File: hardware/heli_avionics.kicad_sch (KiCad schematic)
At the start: 13 parts, among them J1 UPDI, SW1 Reset, U1 ATmega4808-A, U5 BMP390L

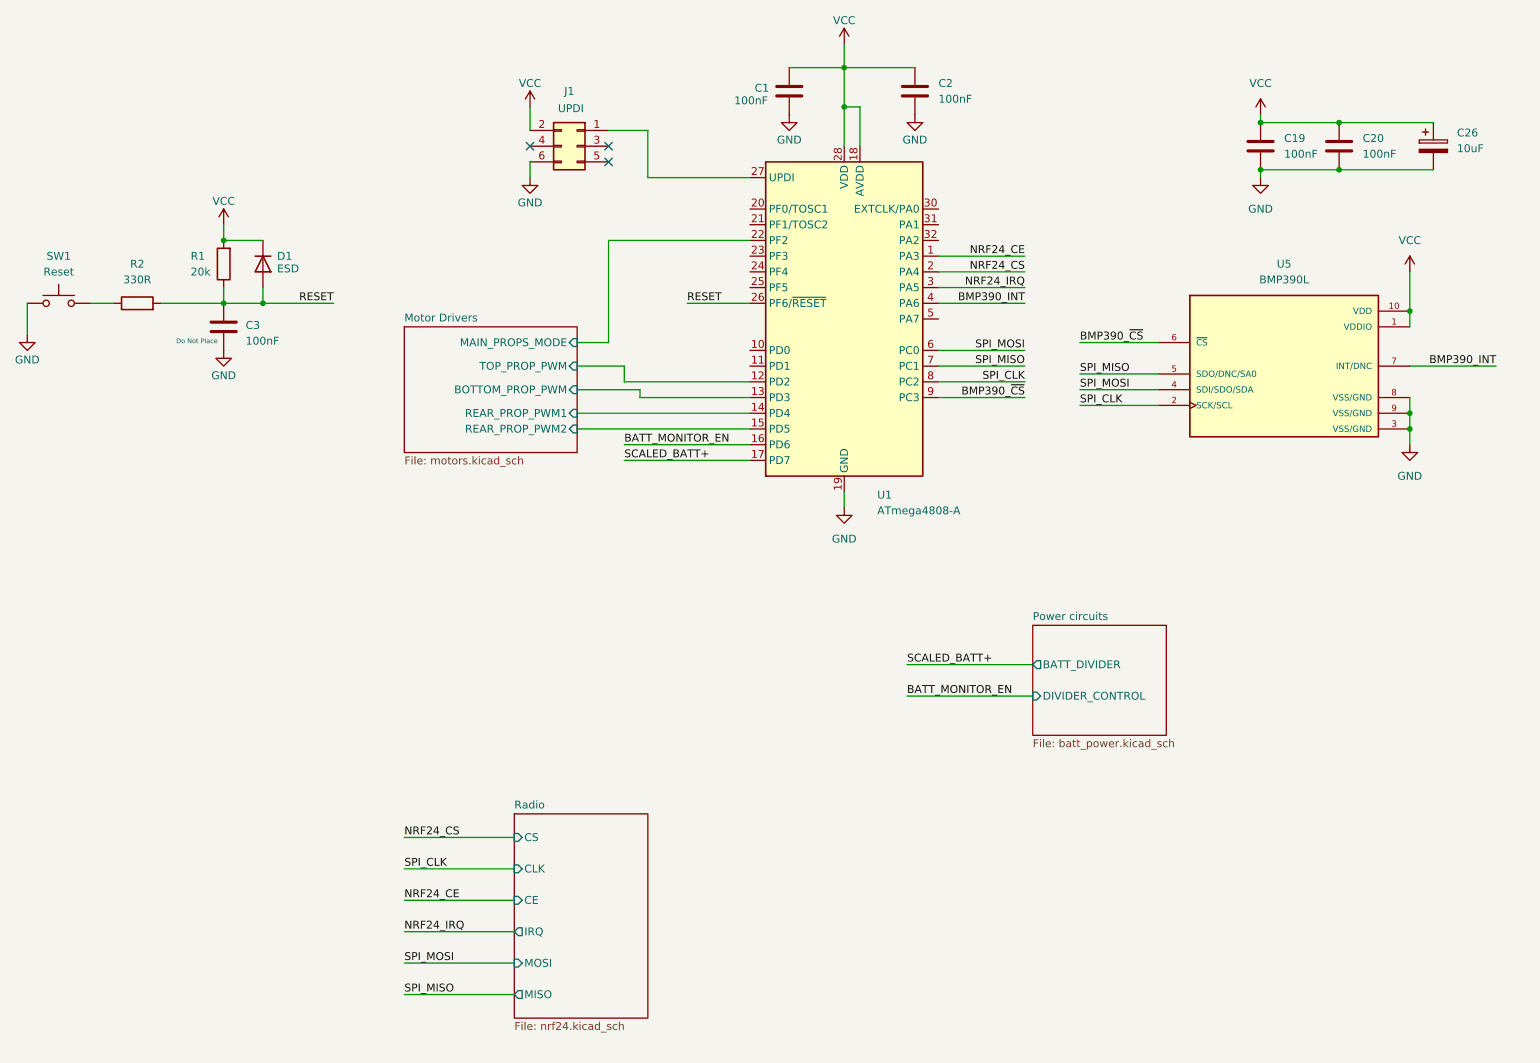
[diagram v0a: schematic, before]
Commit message: Tidy net names & move BMP390 to subsheet
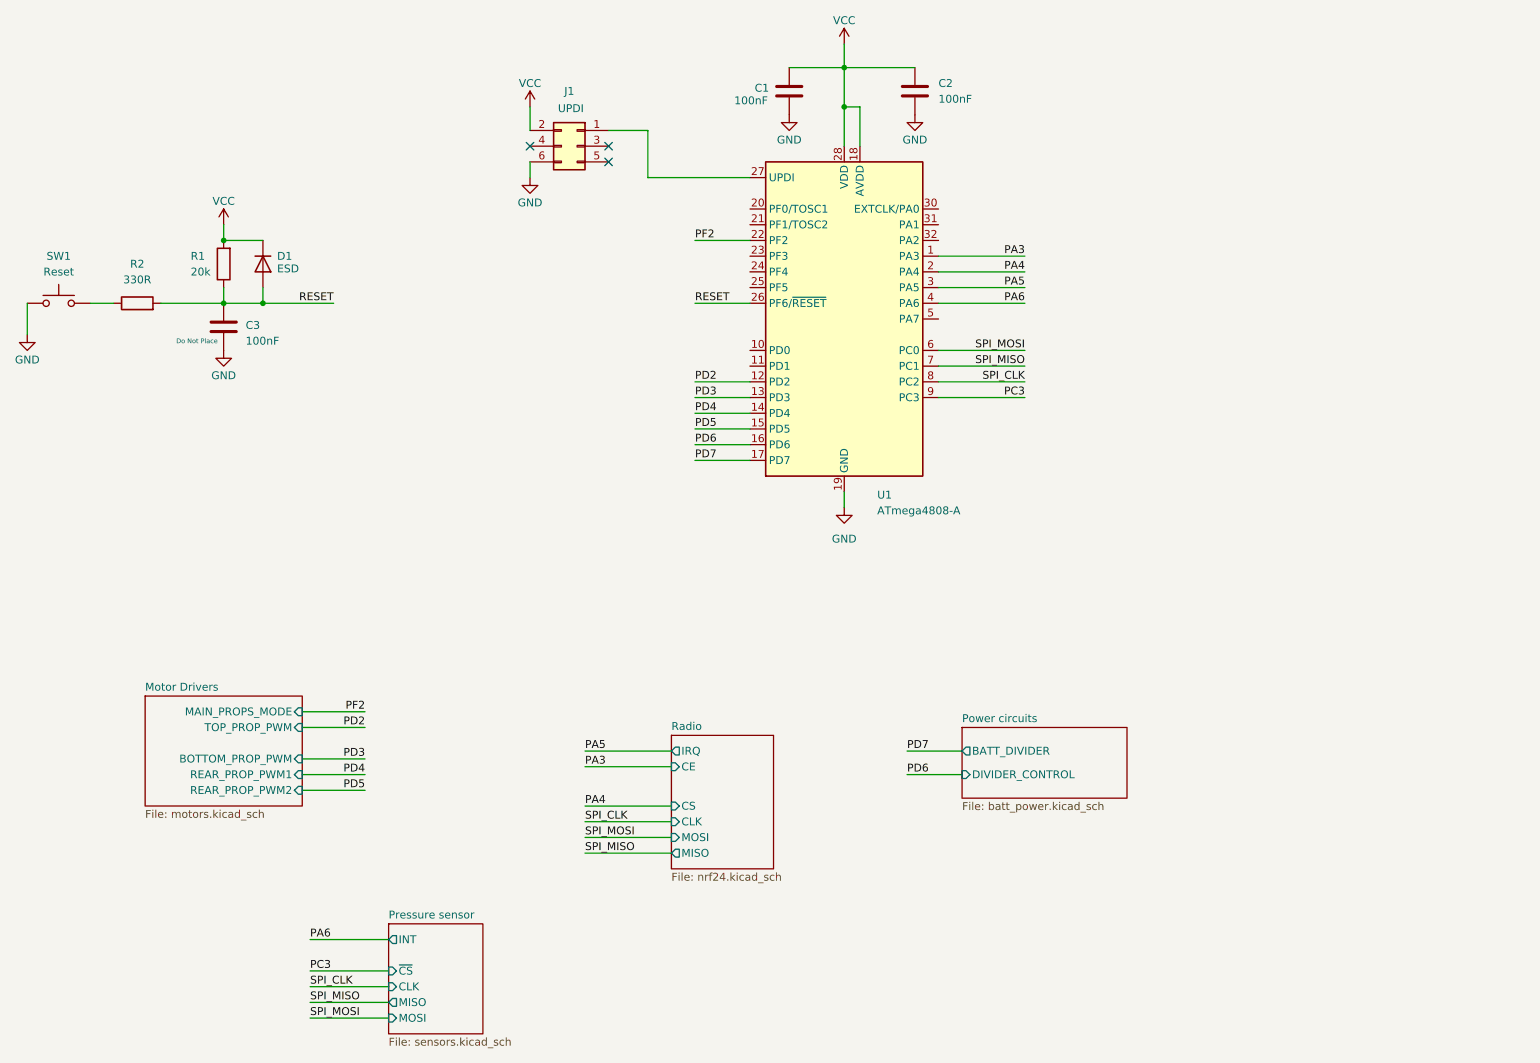
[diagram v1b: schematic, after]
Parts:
- removed C19, C20: 100nF, symbol Device:C
- removed C26: 10uF, symbol Device:C_Polarized
- removed U5: BMP390L, heli-footprints:BMP390L, symbol heli_symbols:BMP390L
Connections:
- net BATT_MONITOR_EN renamed PD6
- net BMP390_INT renamed PA6
- net BMP390_~{CS} renamed PC3
- net Motor Drivers/BOTTOM_PROP_PWM renamed PD3
- net Motor Drivers/MAIN_PROPS_MODE renamed PF2
- net Motor Drivers/REAR_PROP_PWM1 renamed PD4
- net Motor Drivers/REAR_PROP_PWM2 renamed PD5
- net Motor Drivers/TOP_PROP_PWM renamed PD2
- net NRF24_CE renamed PA3
- net NRF24_CS renamed PA4
- net NRF24_IRQ renamed PA5
- net SCALED_BATT+ renamed PD7
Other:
- added sheet Pressure sensor (sensors.kicad_sch)

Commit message: Added UART and LED
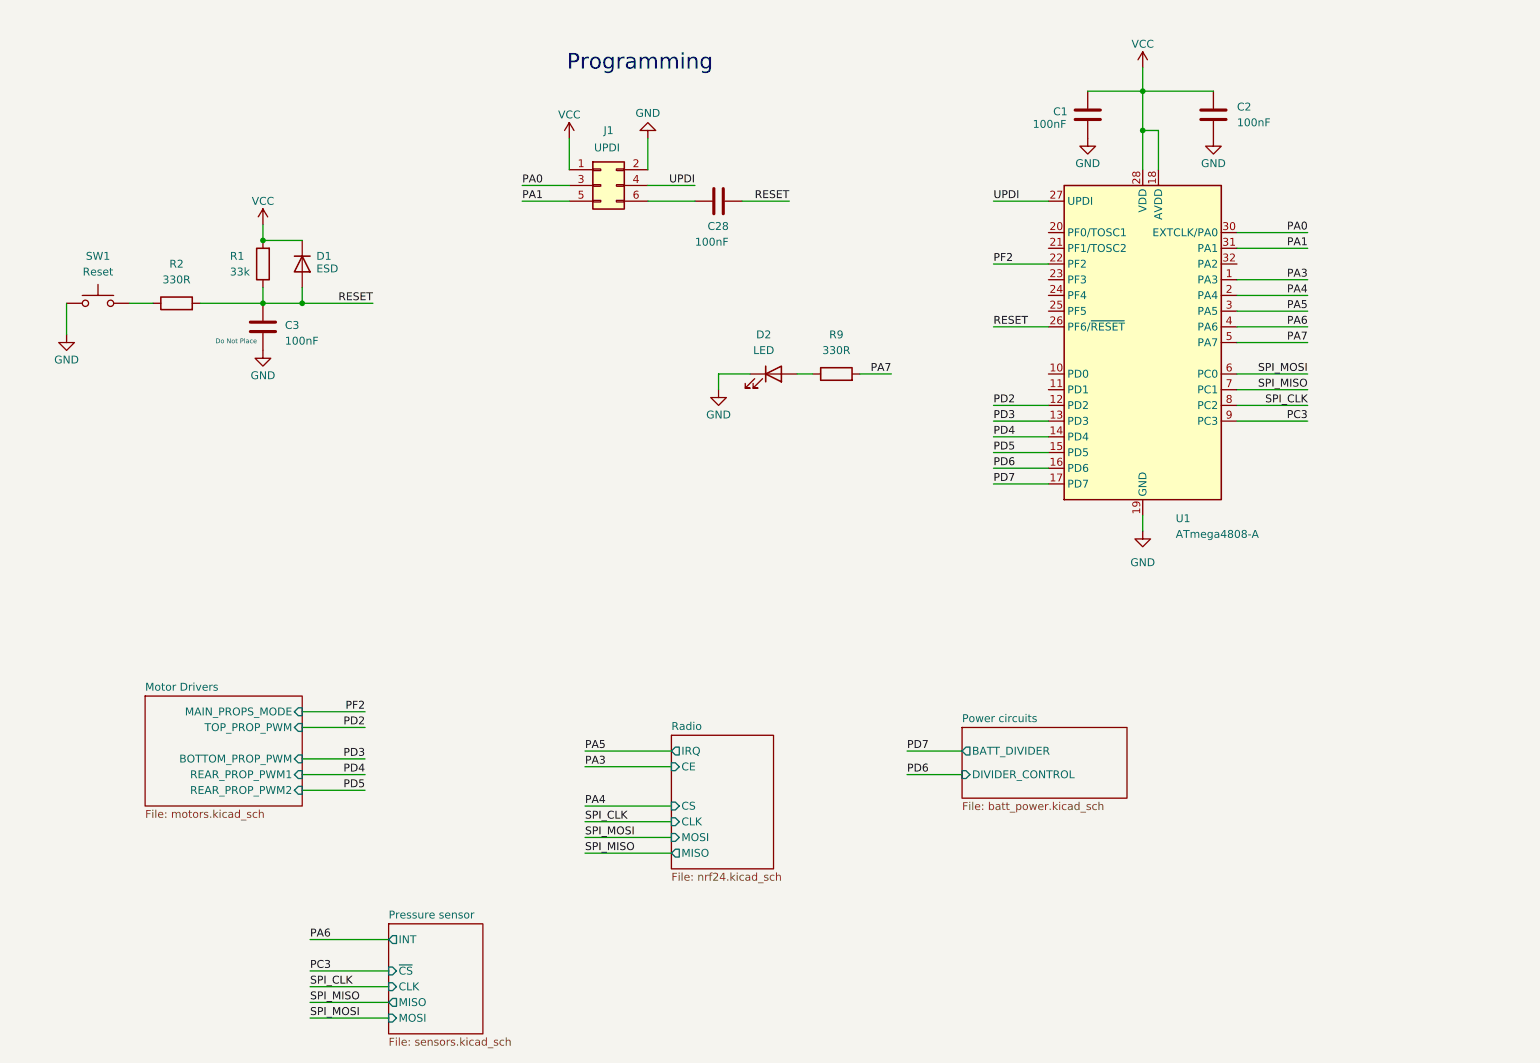
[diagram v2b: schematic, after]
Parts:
- added C28: 100nF, symbol Device:C
- added D2: LED, symbol Device:LED
- added R9: 330R, symbol Device:R
- R1: value 20k -> 33k
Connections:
- net GND: now also J1.2 (Pin_2), D2.1 (K); no longer J1.6 (Pin_6)
- net RESET: now also C28.1
- net VCC: now also J1.1 (Pin_1); no longer J1.2 (Pin_2)
- net UPDI: now reaches U1.27 (UPDI)
- net UPDI: now also J1.4 (Pin_4); no longer J1.1 (Pin_1)
- net PA0: now reaches J1.3 (Pin_3)
- net PA0: now also U1.30 (EXTCLK/PA0)
- net PA1: now reaches J1.5 (Pin_5)
- net PA1: now also U1.31 (PA1)
- net PA7: now reaches U1.5 (PA7)
- net PA7: now also R9.2
- new net: C28.2, J1.6 (Pin_6)
- new net: D2.2 (A), R9.1
- no-connect marks 3 -> 0
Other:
- note added: "Programming"
- moved on the sheet: C1, C2, C3, D1, J1, R1, R2, SW1, U1

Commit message: Added chassis LED connector
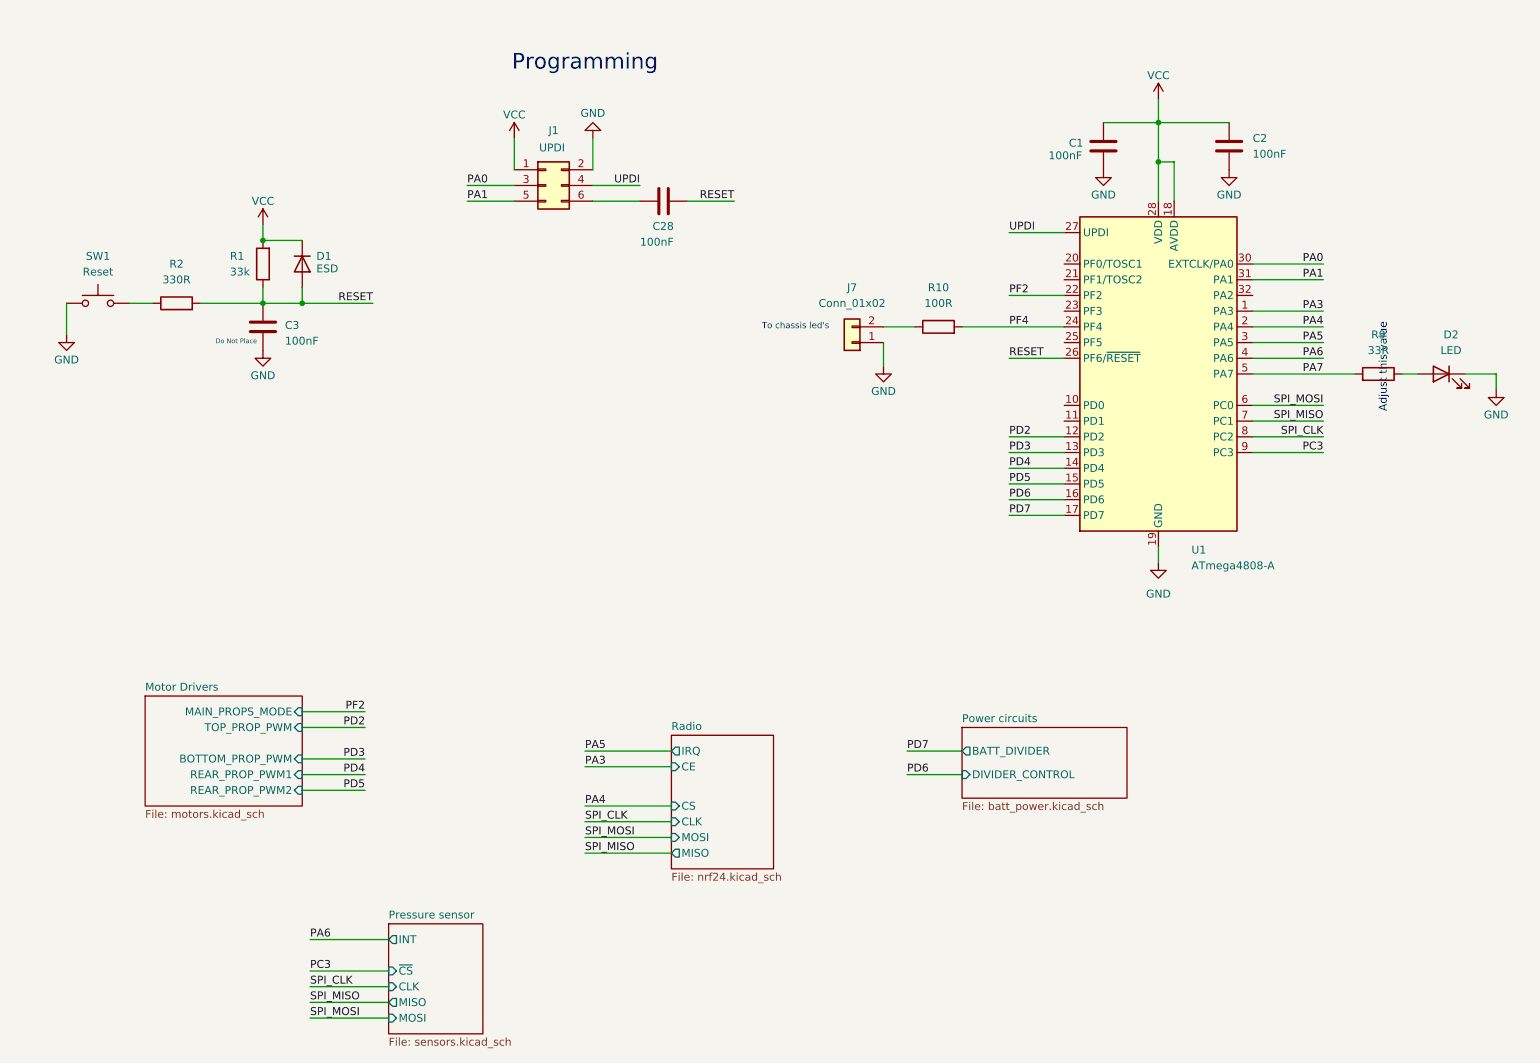
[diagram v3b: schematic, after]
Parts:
- added J7: Conn_01x02, symbol Connector_Generic:Conn_01x02
- added R10: 100R, symbol Device:R
- R9: value 330R -> 33R
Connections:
- net GND: now also J7.1 (Pin_1)
- net PF4: now reaches U1.24 (PF4)
- net PF4: now also R10.2
- new net: J7.2 (Pin_2), R10.1
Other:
- note added: "Adjust this value"
- note added: "To chassis led's"
- moved on the sheet: C1, C2, C28, D2, J1, R9, U1

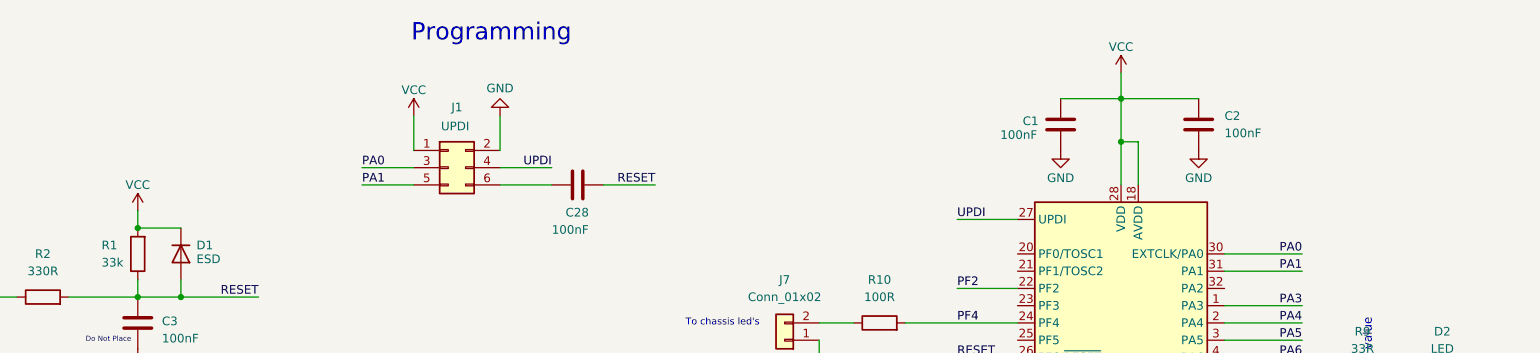
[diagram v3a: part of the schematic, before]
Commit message: Updated decoupling caps
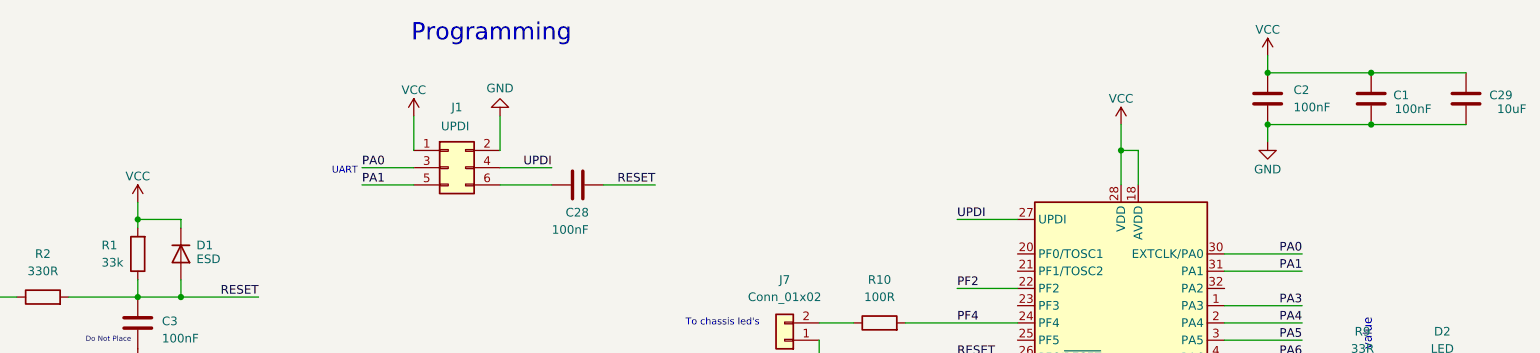
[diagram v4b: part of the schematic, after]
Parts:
- added C29: 10uF, symbol Device:C
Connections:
- net GND: now also C29.2
- net VCC: now also C29.1
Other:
- note added: "UART"
- moved on the sheet: C1, C2
